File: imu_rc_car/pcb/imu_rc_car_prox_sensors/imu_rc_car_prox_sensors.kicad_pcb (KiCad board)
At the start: 2 copper layers, 23.6 x 24 mm, 16 parts, among them J1 Conn_01x03_Socket, U1 LMV358

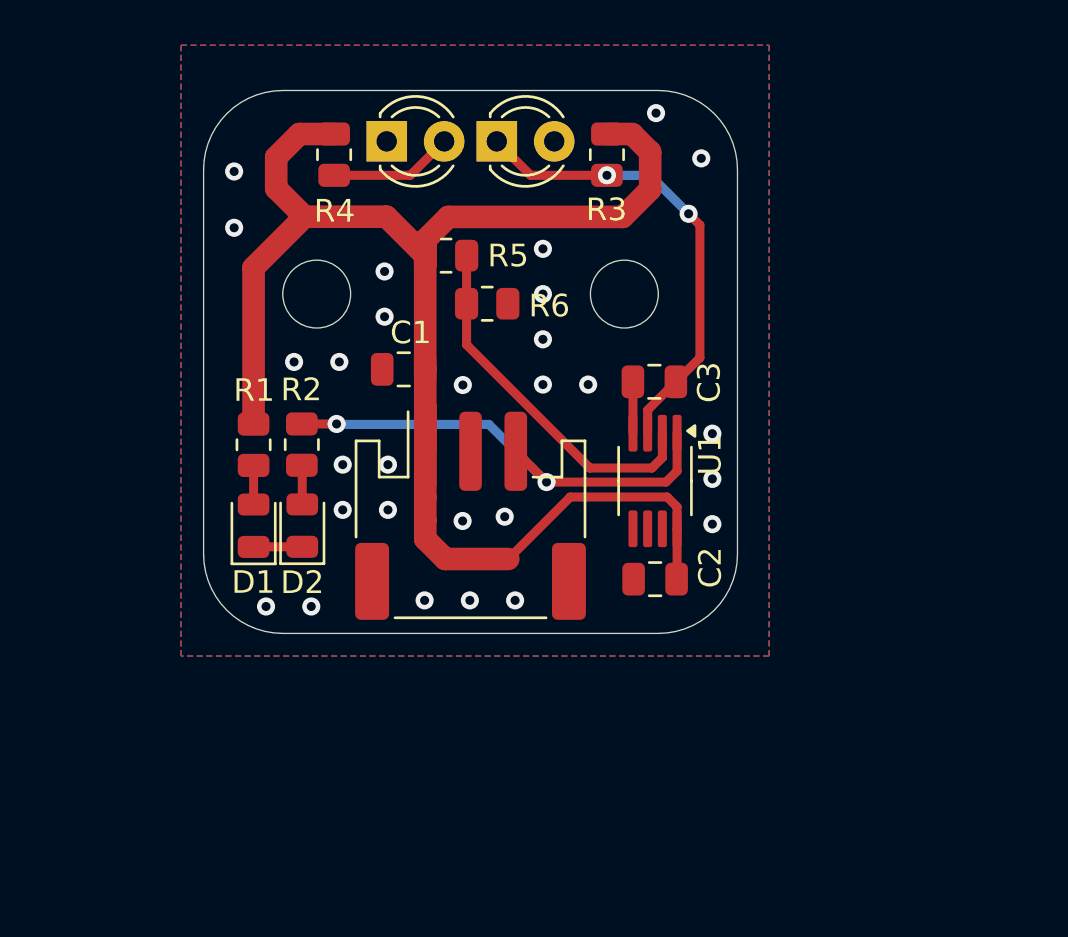
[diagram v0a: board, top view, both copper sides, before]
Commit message: commit #23
minor changes to chassis 3d file
added proximity sensor 3d casing
v1.1.0 prox sensor board, featuring a band-pass filter and clk input
minor formatting to the src code
added function to update RSSI bars
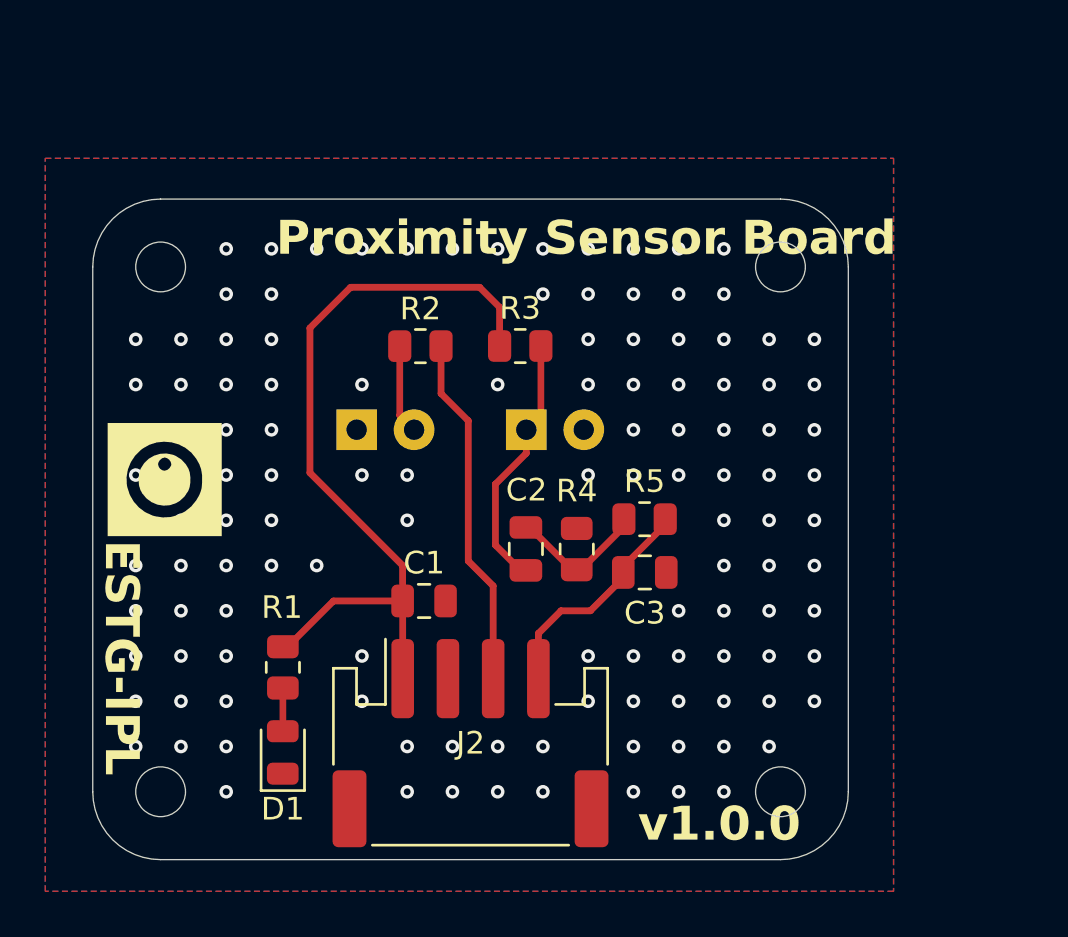
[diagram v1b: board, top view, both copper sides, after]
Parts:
- removed D4: AA, LED_THT:LED_D3.0mm_IRBlack
- removed J1: Conn_01x03_Socket, Connector_JST:JST_PH_S3B-PH-SM4-TB_1x03-1MP_P2.00mm_Horizontal
- removed R6: R_US, Resistor_SMD:R_0805_2012Metric
- removed U1: LMV358, Package_SO:MSOP-8_3x3mm_P0.65mm
- added J2: Conn_01x04_Socket, IMURCLibrary:JST_PH_S4B-PH-SM4-TB_1x04-1MP_P2.00mm_Horizontal, F.Cu at (106.8, 89.8)
- C3: value 10nF -> 1nF
- D2: value LED -> IR204A; footprint LED_SMD:LED_0805_2012Metric -> LED_THT:LED_D5.0mm_Horizontal_O1.27mm_Z3.0mm_Clear; moved to B.Cu
- D3: value IR204A -> AA; footprint LED_THT:LED_D3.0mm_IRBlack -> LED_THT:LED_D5.0mm_Horizontal_O1.27mm_Z3.0mm_IRBlack; moved to B.Cu
- G***: moved to F.Cu
- R2: value 1k -> 180
- R4: value 180 -> 43 (1%)
- R5: value R_US -> 4k02 (1%)
- moved R4 20.5 mm to (111.5, 81.3), turned to -90 degrees
- moved G*** 19.6 mm to (93.3, 78.2), turned to -90 degrees
- moved R5 14.6 mm to (114.5, 80.0)
- moved D3 14.2 mm to (109.3, 76.0)
- moved C1 10.3 mm to (104.7, 83.6), turned to 0 degrees
- moved D1 10.1 mm to (98.5, 90.3)
- moved R1 9.92 mm to (98.5, 86.5)
- moved R3 9.29 mm to (109.0, 72.3), turned to 180 degrees
- moved C3 8.44 mm to (114.5, 82.3)
- moved R2 6.81 mm to (104.6, 72.3), turned to 0 degrees
- moved C2 5.87 mm to (109.2, 81.3), turned to 90 degrees
- moved D2 4.87 mm to (101.8, 76.0), turned to 0 degrees
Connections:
- C2 pad 1: +3V3 -> Net-(D3-K)
- C2 pad 2: GND -> Net-(C2-Pad2)
- C3 pad 1: Net-(D4-K) -> GND
- C3 pad 2: GND -> AOUT
- D3 pad 1: GND -> Net-(D3-K)
- D3 pad 2: Net-(D3-A) -> GND
- R2 pad 2: OUT -> CLK
- R3 pad 1: Net-(D4-K) -> Net-(D3-K)
- R4 pad 1: Net-(D3-A) -> GND
- R4 pad 2: +3V3 -> Net-(C2-Pad2)
- R5 pad 1: Net-(U1A--) -> AOUT
- R5 pad 2: +3V3 -> Net-(C2-Pad2)
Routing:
- net +3V3: track 72.1 -> 34.5 mm
- net OUT: track 21.4 -> 0.00 mm, vias 2 -> 0
- net Net-(D4-K): track 20.7 -> 0.00 mm, vias 2 -> 0
- net Net-(U1A--): track 16.1 -> 0.00 mm
- net CLK: track 0.00 -> 15.7 mm
- net Net-(D3-K): track 0.00 -> 11.4 mm
- net AOUT: track 0.00 -> 10.1 mm
- net Net-(C2-Pad2): track 0.00 -> 6.23 mm
- net Net-(D3-A): track 5.49 -> 0.00 mm
- net GND: track 4.43 -> 0.06 mm, vias 28 -> 124
- net Net-(D2-A): track 1.74 -> 3.96 mm
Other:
- board size 23.6 x 24 mm -> 33.4 x 29.2 mm
- board text added: "{ "ViaStitching": "0.2", "stitch_zone_0": { "HSpacing": "2", "VSpacing": "2", "HOffset": "0", "VOffset": "0", "Clearance": "0.5", "Randomize": false } }"

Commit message: commit #24
version 2 of proximity sensor case (better results)
updated all M2 holes in pcbs to 2.4mm diameter instead of 2.2mm
updated all M3 holes in pcbs to 3.4mm diameter instead of 3.2mm
minor changes to encoder board
gerber files encoder board
first revision in hand unit
added prox sensor test unit (for test purposes)
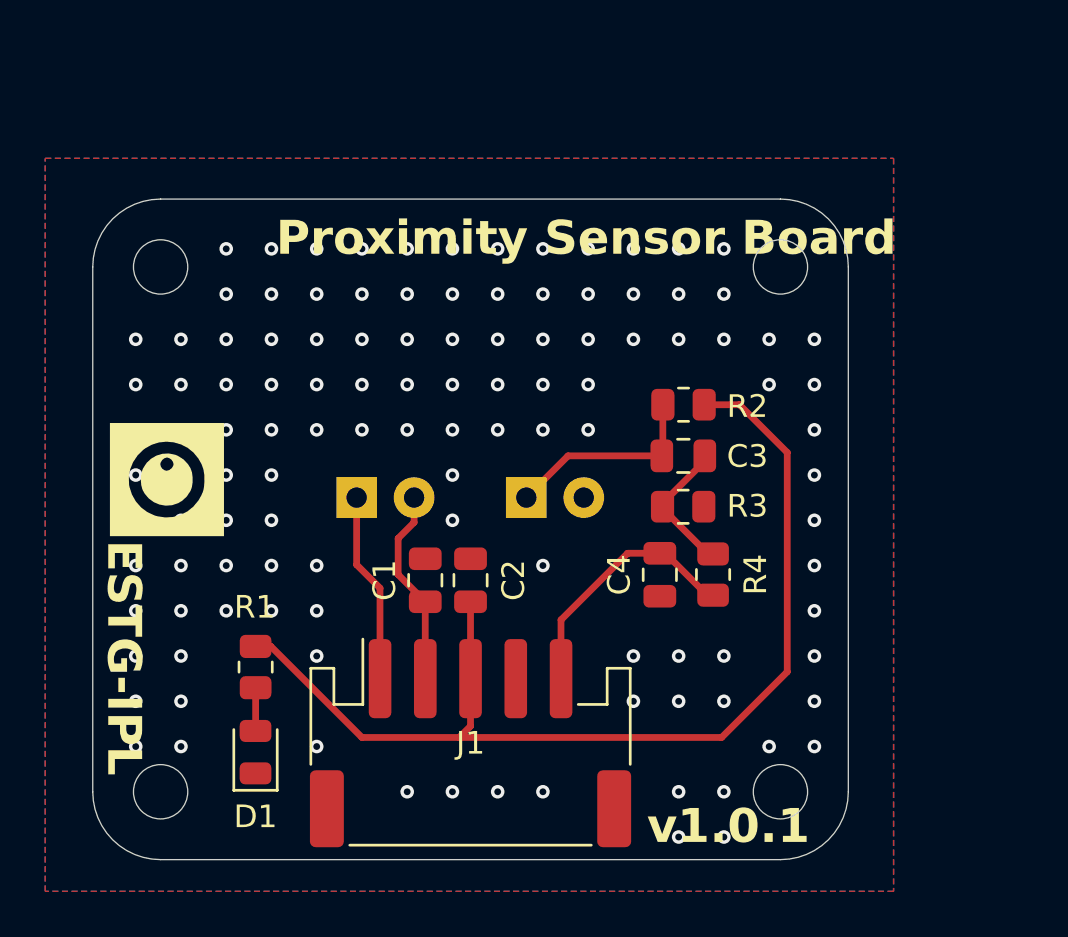
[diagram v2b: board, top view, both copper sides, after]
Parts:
- removed J2: Conn_01x04_Socket, IMURCLibrary:JST_PH_S4B-PH-SM4-TB_1x04-1MP_P2.00mm_Horizontal
- removed the R2 at (104.6, 72.3)
- added C2: 10uF, Capacitor_SMD:C_0805_2012Metric, F.Cu at (106.8, 82.7)
- added J1: Conn_01x05_Socket, IMURCLibrary:JST_PH_S5B-PH-SM4-TB_1x05-1MP_P2.00mm_Horizontal, F.Cu at (106.8, 89.8)
- moved C3 8.08 mm to (116.2, 77.2), turned to 0 degrees
- moved R2 7.67 mm to (116.2, 74.9), turned to 0 degrees
- moved R3 5.06 mm to (116.2, 79.4), turned to 180 degrees
- moved R4 3.89 mm to (117.5, 82.4), turned to 90 degrees
- moved D2 3.00 mm to (101.8, 79.0)
- moved D3 3.00 mm to (109.3, 79.0)
- moved D1 1.21 mm to (97.3, 90.2)
- moved R1 1.21 mm to (97.3, 86.5)
- moved C1 0.92 mm to (104.8, 82.7), turned to -90 degrees
- moved C4 0.67 mm to (115.2, 82.4), turned to 90 degrees
- moved G*** 0.10 mm to (93.4, 78.2)
- renumbered C2 to C3, C3 to C4, R3 to R2, R4 to R3, R5 to R4
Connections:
- net AOUT renamed AO
- C1 pad 1: +3V3 -> GND
- C1 pad 2: GND -> SI
- D2 pad 1: GND -> SO
- D2 pad 2: Net-(D2-A) -> SI
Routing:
- net CLK: track 15.7 -> 0.00 mm
- net +3V3: track 34.5 -> 46.8 mm
- net SI: track 0.00 -> 8.79 mm
- net SO: track 0.00 -> 8.43 mm
- net Net-(D2-A): track 3.96 -> 0.00 mm
- net Net-(D3-K): track 11.4 -> 9.04 mm
- net AO: track 10.1 -> 11.3 mm
- net GND: track 0.06 -> 0.00 mm, vias 124 -> 116
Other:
- outline, holes or cut-outs redrawn
- board text added: "v1.0.1"
- board text added: "{ "ViaStitching": "0.2", "stitch_zone_0": { "HSpacing": "2", "VSpacing": "2", "HOffset": "0", "VOffset": "0", "Clearance": "0", "Randomize": false } }"
- board text removed: "v1.0.0"
- board text removed: "{ "ViaStitching": "0.2", "stitch_zone_0": { "HSpacing": "2", "VSpacing": "2", "HOffset": "0", "VOffset": "0", "Clearance": "0.5", "Randomize": false } }"

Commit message: commit #25
added library for mouse-bites
minor changes in prox sensors board
added necessary changes for test unit to print
minor changes in hand unit
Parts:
- moved R4 3.94 mm to (118.3, 78.5), turned to 0 degrees
- moved R3 3.83 mm to (119.4, 81.6), turned to 90 degrees
- moved D3 2.36 mm to (111.1, 77.5)
- moved D2 2.35 mm to (100.0, 77.5)
- moved C4 2.17 mm to (117.2, 81.6)
- moved C3 2.14 mm to (118.3, 76.5)
- moved R2 2.08 mm to (118.3, 74.5)
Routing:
- net +3V3: track 46.8 -> 40.6 mm
- net SI: track 8.79 -> 11.1 mm
- net SO: track 8.43 -> 10.7 mm
- net Net-(C3-Pad2): track 6.17 -> 4.22 mm
- net AO: track 11.3 -> 13.2 mm
- net Net-(D3-K): track 9.04 -> 10.6 mm
- net GND: vias 116 -> 121
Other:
- board text removed: "{ "ViaStitching": "0.2", "stitch_zone_0": { "HSpacing": "2", "VSpacing": "2", "HOffset": "0", "VOffset": "0", "Clearance": "0", "Randomize": false } }"

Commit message: commit #30
changed 3d model offset in esp32s3
imported mouse-bites to kicad
final changes in imu-rc car before revision
critical change in pins 3 and 4 of optical sensor which were switched (encoder board)
removed test unit
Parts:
- renumbered D3 to Rx, D2 to Tx
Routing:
- net GND: vias 121 -> 114
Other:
- board text added: "IMU-RC"
- board text added: "v1.0.0"
- board text removed: "v1.0.1"

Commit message: commit #32
costs table 4
first revision of imu rc car pcb
imu rc encoders final version v1.0.0 (ordered)
imu rc prox sensors final version v1.0.0 (ordered)
minor resistors tolerance changes in hand unit
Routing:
- net GND: vias 114 -> 93
